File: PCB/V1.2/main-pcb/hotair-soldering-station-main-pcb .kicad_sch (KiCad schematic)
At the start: 126 parts, among them J1 230VAC_IN, J10 T12_power (NS-25 r2,54), J11 LCD_CON2 (JST r.2.0), J12 LCD_CON1 (JST r.2.0), J13 ICP (goldpin r2,54), J2 FRONT_PANEL (IDC r. 2,54), J3 EARTH_GND, J4 24V_IN (NS-25 r2,54), J5 PSUPPLY (PWZ-02S r.3,96), J6 HOTAIR_FAN (JST r,2,54), J7 HOTAIR_MEAS (JST r.2,5), J8 HOTAIR_HEATER (PWZ-02S r.3,96), J9 WEP (r.2,54), Q1 BC817, Q10 RFP15P05, Q11 BC817, Q12 BC817, Q13 BC817, Q14 BC807, Q15 RFP15P05, Q2 BC807, Q3 BC817, Q4 RFP15P05, Q5 BC817, Q6 BT139-600, Q7 BC817, Q8 BC807, Q9 BC817, U1 MOC3041M, U2 MAX31855KASA, U3 MP1584-Step-Down, U4 AP1117-ADJ, U6 LM358, U8 STM32F103C6Tx

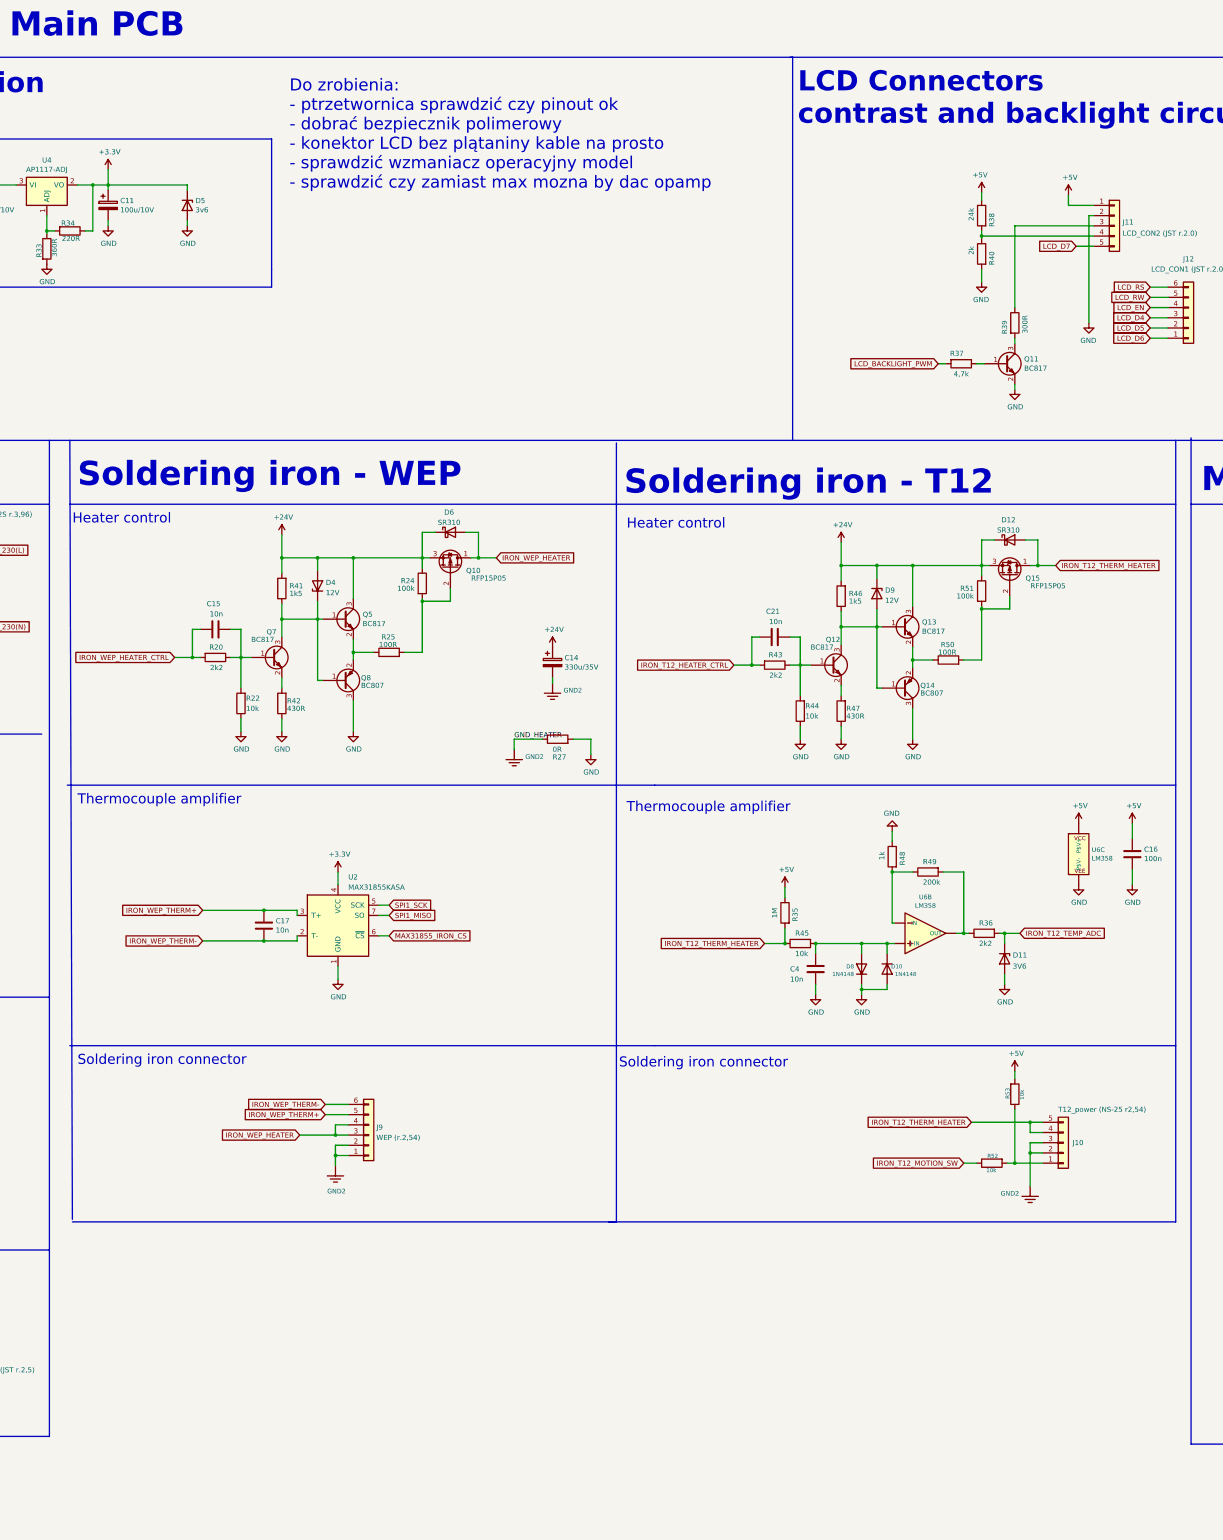
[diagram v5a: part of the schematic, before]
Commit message: Alternative thermocouple amplifier for WEP
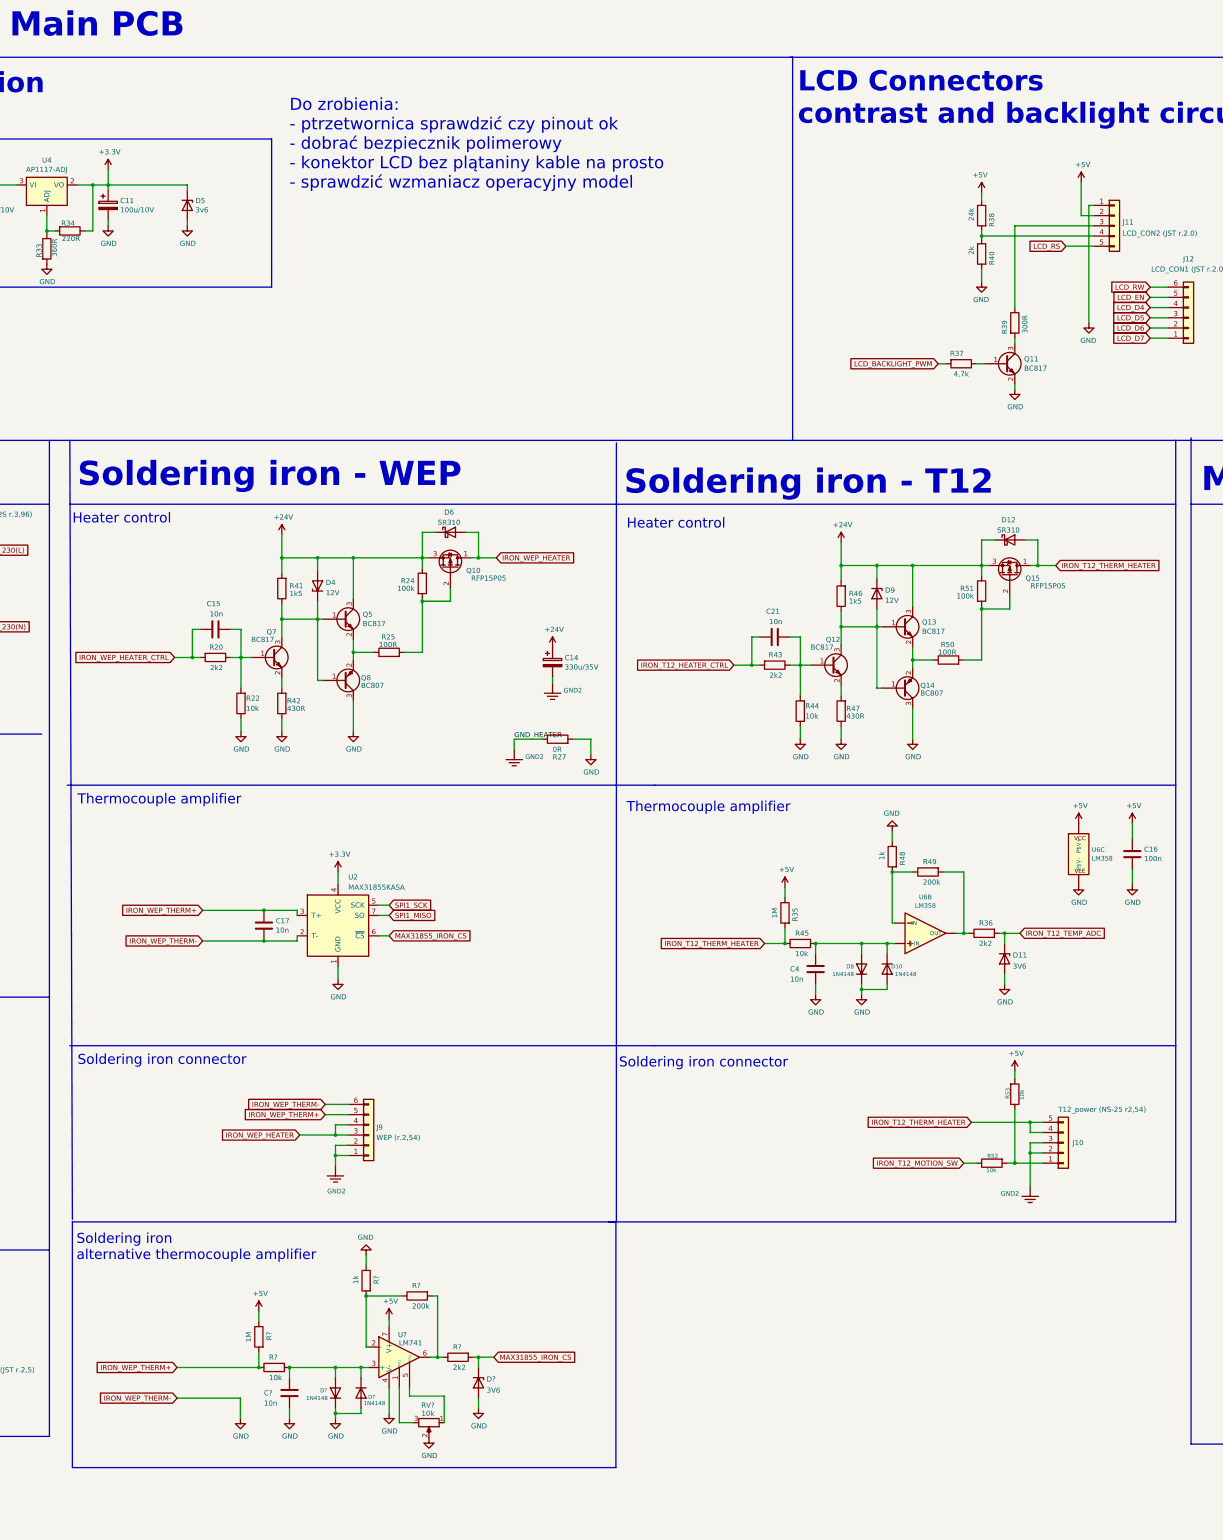
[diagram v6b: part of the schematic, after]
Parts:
- added C?: 10n, Capacitors:0805, symbol Device:C
- added D? (x2): 1N4148, Diode_SMD:D_MiniMELF, symbol Device:D
- added D?: 3V6, Diode_SMD:D_MiniMELF, symbol Device:D_Zener
- added R?: 1M, Capacitors:0805, symbol Device:R
- added R?: 200k, Capacitors:0805, symbol Device:R
- added R?: 1k, Capacitors:0805, symbol Device:R
- added R?: 2k2, Capacitors:0805, symbol Device:R
- added R?: 10k, Capacitors:0805, symbol Device:R
- added RV?: 10k, symbol Device:R_Potentiometer
- added U?: LM741, Package_SO:SO-8_3.9x4.9mm_P1.27mm, symbol Amplifier_Operational:LM741
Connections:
- net IRON_WEP_THERM- is gone; now on net GND: C17.2, J9.6 (Pin_6), U2.2 (T-)
- net +5V: now also J11.2 (Pin_2), R?.1, U?.7 (V+); no longer J11.1 (Pin_1)
- net GND: now also J11.1 (Pin_1), C?.2, D?.1 (K), D?.2 (A), D?.2 (A), R?.1, RV?.2, U?.4 (V-); no longer J11.2 (Pin_2)
- net IRON_WEP_THERM+: now also R?.1, R?.2
- net LCD_D4: now also J12.4 (Pin_4); no longer J12.3 (Pin_3)
- net LCD_D5: now also J12.3 (Pin_3); no longer J12.2 (Pin_2)
- net LCD_D6: now also J12.2 (Pin_2); no longer J12.1 (Pin_1)
- net LCD_D7: now also J12.1 (Pin_1); no longer J11.5 (Pin_5)
- net LCD_EN: now also J12.5 (Pin_5); no longer J12.4 (Pin_4)
- net LCD_RS: now also J11.5 (Pin_5); no longer J12.6 (Pin_6)
- net LCD_RW: now also J12.6 (Pin_6); no longer J12.5 (Pin_5)
- net MAX31855_IRON_CS: now also D?.1 (K), R?.2
- new net: RV?.3, U?.1 (NULL)
- new net: R?.1, R?.2, U?.2 (-)
- new net: C?.1, D?.1 (K), D?.2 (A), R?.2, U?.3 (+)
- new net: RV?.1, U?.5 (NULL)
- new net: R?.1, R?.2, U?.6
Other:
- note added: "Do zrobienia: - ptrzetwornica sprawdzić czy pinout ok - dobrać bezpiecznik polimerowy - konektor LCD bez plątaniny kable na prosto - sprawdzić wzmaniacz operacyjny model"
- note added: "Soldering iron alternative thermocouple amplifier"
- note removed: "Do zrobienia: - ptrzetwornica sprawdzić czy pinout ok - dobrać bezpiecznik polimerowy - konektor LCD bez plątaniny kable na prosto - sprawdzić wzmaniacz operacyjny model - sprawdzić czy zamiast max mozna by dac opamp"

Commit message: All knowned problems fixed on schematic, routing mains voltage section
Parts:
- removed U3: MP1584-Step-Down, My-Footprints:MP1584_Mini_3A_Step_Down_Conv, symbol hotair-soldering-station-main-pcb-rescue:MP1584-Step-Down-My-Lib
- added J14: Unused_GPIO, My-Footprints:WIRE_PAD_1,3mm, symbol Connector_Generic:Conn_01x01
- added R57: 47k, Capacitors:0805, symbol Device:R
- added R58: 0R, Resistors:0805, symbol Device:R
- added U3: MP1584-Step-Down, My-Footprints:MP1584_Mini_3A_Step_Down_Conv, symbol My-Lib:MP1584-Step-Down
- J3: value EARTH_GND -> (none); footprint My-Footprints:Screw-Terminal-5.00mm-3pin -> (none)
- R21: value 200R -> (none); footprint Resistors_ThroughHole:R_Axial_DIN0207_L6.3mm_D2.5mm_P10.16mm_Horizontal -> (none)
- RV1: renamed from RV?; footprint (none) -> Potentiometer_THT:Potentiometer_Bourns_3296W_Vertical
- U6: value LM358 -> AD8606
- gave numbers to parts that had none: 10
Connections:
- net +24V: now also U3.1 (IN+)
- net +5V: now also U3.3 (OUT+)
- net GND: now also R57.1, R58.2, U3.2 (IN-), U3.4 (OUT-); no longer C17.2, J9.6 (Pin_6), U2.2 (T-)
- net LCD_D4: now also J12.2 (Pin_2); no longer J12.4 (Pin_4)
- net LCD_D6: now also J12.4 (Pin_4); no longer J12.2 (Pin_2)
- net LCD_D7: now also J12.5 (Pin_5); no longer J12.1 (Pin_1)
- net LCD_EN: now also J12.1 (Pin_1); no longer J12.5 (Pin_5)
- net LCD_RS: now also J11.4 (Pin_4); no longer J11.5 (Pin_5)
- net LCD_RW: now also J11.5 (Pin_5); no longer J12.6 (Pin_6)
- net at C1.1, Q2.1 (B), R2.2: now also R57.2
- net UNUSED_GPIO: now reaches U8.14 (PA4)
- net UNUSED_GPIO: now also J14.1 (Pin_1)
- net at R39.1: now also J12.6 (Pin_6); no longer J11.3 (Pin_3)
- net at R38.2, R40.1: now also J11.3 (Pin_3); no longer J11.4 (Pin_4)
- new net IRON_WEP_THERM-: C17.2, J9.6 (Pin_6), R58.1, U2.2 (T-)
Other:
- note removed: "Do zrobienia: - ptrzetwornica sprawdzić czy pinout ok - dobrać bezpiecznik polimerowy - konektor LCD bez plątaniny kable na prosto - sprawdzić wzmaniacz operacyjny model"
- note removed: "TIM14CH1 - Output compare (buzer)"
- note removed: "TIM3_CH2 - PWM"
- moved on the sheet: C1, C2, D7, J11, J12, LS1, Q11, Q2, Q3, Q4, Q9, R10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
